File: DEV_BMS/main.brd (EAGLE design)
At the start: 93 x 70 mm, 75 parts

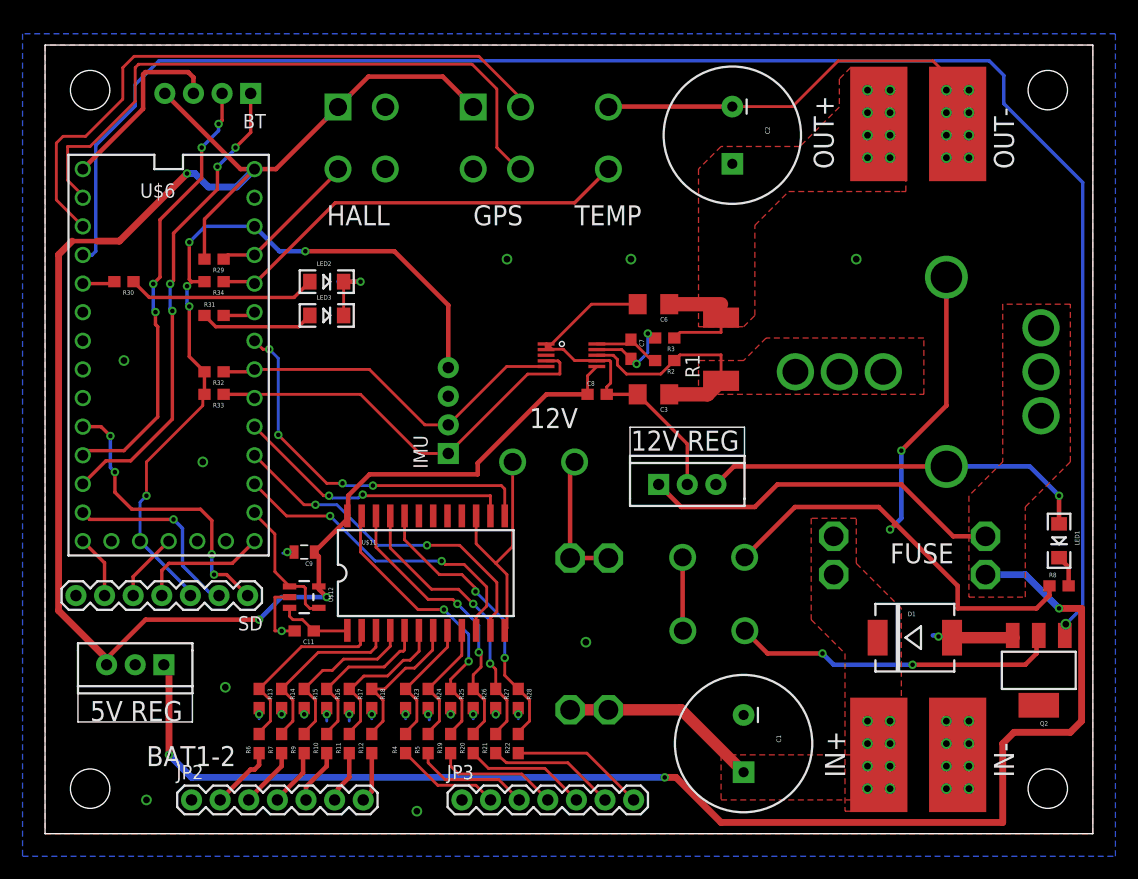
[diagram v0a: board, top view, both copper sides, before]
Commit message: new BMS with CAN and NRF24 radio
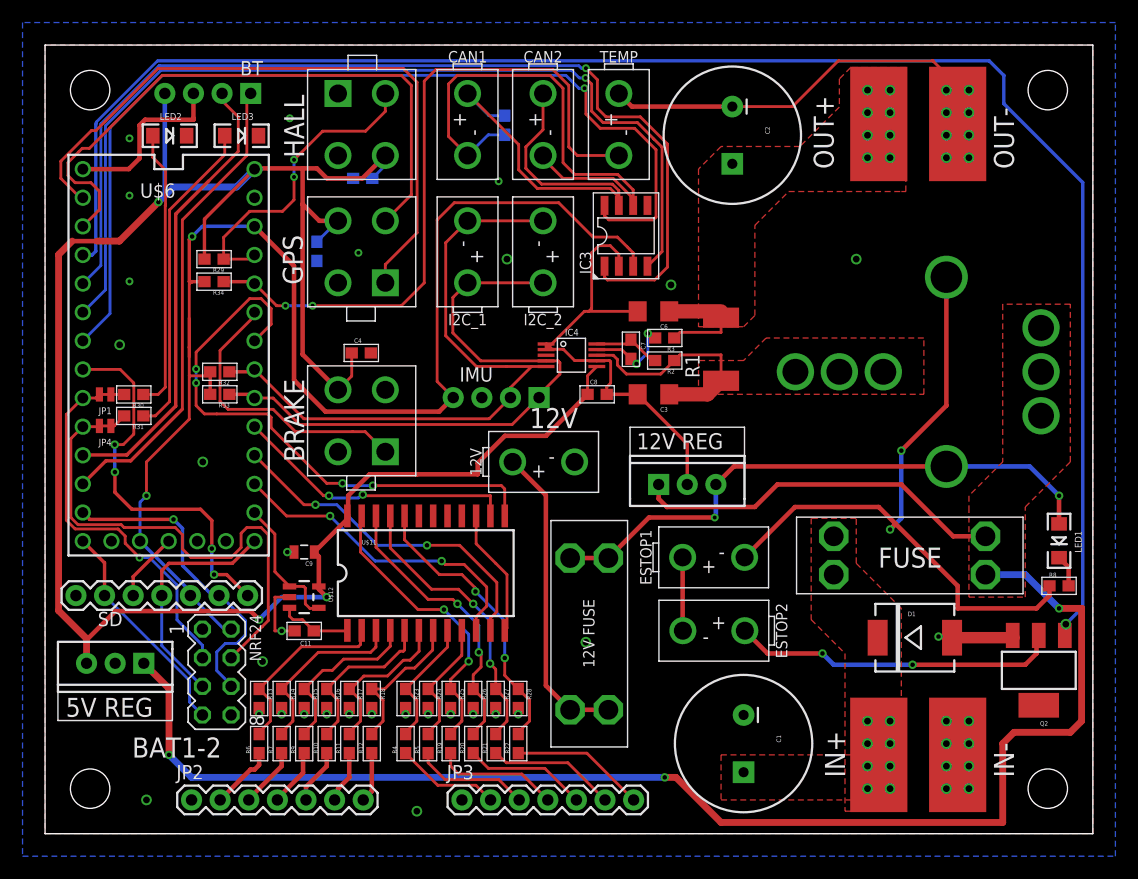
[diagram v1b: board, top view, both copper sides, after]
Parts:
- added BRAKE: HEADER4VALULOK, Custom_old:4PINVALULOK
- added C10, C5: 1uF, SparkFun-Passives:0603-CAP
- added C4: 4.7uF, SparkFun-Passives:0603-CAP
- added CAN1, CAN2, I2C_1, I2C_2, TEMP: HEADER2, Custom_old:2PINVALULOK
- added IC3: SN65HVD230D, Misaka-IC:SO-8
- added JP1, JP4: JUMPER-SMT_2_NC_TRACE_NO-SILK, SparkFun-Jumpers:SMT-JUMPER_2_NC_TRACE_NO-SILK
- added NRF24: (no value), con-lstb:MA04-2
- added R36: 120, SparkFun-Passives:0603-RES
- U$17: value HEADER2 -> (none); device Custom_old:2PINVALULOK -> Custom_old:DEV
- moved U$17 21.5 mm to (68.6, 48.3), flipped to the bottom
- moved LED2 19.0 mm to (11.1, 62.0)
- moved LED3 17.6 mm to (17.4, 62.0)
- moved R31 11.4 mm to (7.87, 37.1), turned to 180 degrees
- moved R30 10.0 mm to (7.87, 39.0)
- moved IMU 9.46 mm to (43.8, 38.7), turned to 180 degrees
- moved GPS 9.06 mm to (30.2, 54.4), turned to 180 degrees
- moved IC1 1.78 mm to (6.22, 15.1)
- moved HALL 1.20 mm to (26.0, 60.2)
- moved C6 0.63 mm to (54.0, 46.4)
- moved R32 0.51 mm to (15.5, 41.0)
- moved R33 0.51 mm to (15.5, 39.0)
- renumbered U$1 to IC4, U$10 to ESTOP2, U$19 to 12V, U$9 to ESTOP1
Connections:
- removed net N$7: IC2.OUT, LED1.A, U$7.86
- new net 12V: IC2.OUT, LED1.A, U$18.2A, U$18.2B, U$7.86
- new net BRAKE: BRAKE.1, U$6.21/A7
- new net CANH: CAN1.1, CAN2.1, IC3.7, R36.2
- new net CANL: CAN1.2, CAN2.2, IC3.6, R36.1
- new net CAN_RX: IC3.4, U$6.4
- new net CAN_TX: IC3.1, U$6.3
- new net CE: JP1.2, NRF24.3, U$6.7
- new net CSN: JP4.2, NRF24.4, U$6.8
- new net EN_CAN: IC3.8, U$6.5
- new net NRF_INT: NRF24.8
- net 3.3: now also IC3.3, NRF24.2
- net B_RAW: no longer U$18.1A, U$18.1B
- net GND: now also 12V.2, BRAKE.2, C10.2, C4.2, C5.2, GPS.3, HALL.2, IC3.2, NRF24.1, TEMP.1; no longer 12V.1, GPS.2, HALL.3, U$17.1
- net HALL: now also HALL.3; no longer HALL.2
- net LED1: now also JP1.1; no longer U$6.3
- net LED2: now also JP4.1; no longer U$6.21/A7
- net MISO: now also NRF24.7
- net MOSI: now also NRF24.6
- net N$5: now also 12V.1, U$18.1A, U$18.1B; no longer 12V.2, U$18.2A, U$18.2B
- net RX1: now also GPS.1; no longer GPS.4
- net SCK: now also NRF24.5
- net SCL: now also I2C_1.2, I2C_2.2
- net SDA: now also I2C_1.1, I2C_2.1
- net SD_CS: now also U$6.6; no longer U$6.8
- net THERMISTOR: now also TEMP.2; no longer U$17.2
- net TX1: now also GPS.2; no longer GPS.3
- net VCC: now also BRAKE.4, C10.1, C4.1, C5.1, GPS.4, HALL.4; no longer GPS.1, HALL.1
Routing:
- net CAN_TX: track 0.00 -> 89.7 mm, vias 0 -> 1
- net EN_CAN: track 0.00 -> 86.0 mm, vias 0 -> 1
- net CAN_RX: track 0.00 -> 84.2 mm, vias 0 -> 1
- net 12V: track 0.00 -> 52.0 mm, vias 0 -> 2
- net 3.3: track 69.6 -> 120.1 mm, vias 5 -> 2
- net CANL: track 0.00 -> 47.1 mm
- net CSN: track 0.00 -> 44.2 mm
- net CANH: track 0.00 -> 40.4 mm
- net N$7: track 34.7 -> 0.00 mm, vias 1 -> 0
- net CE: track 0.00 -> 33.0 mm, vias 0 -> 1
- net SCL: track 32.9 -> 58.9 mm
- net BRAKE: track 0.00 -> 25.7 mm
- net THERMISTOR: track 38.4 -> 61.7 mm, vias 0 -> 2
- net VCC: track 165.1 -> 186.7 mm
- net N$20: track 10.2 -> 28.5 mm
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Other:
- board text added: "12V FUSE"
- board text added: "BRAKE"
- board text added: "Duke Electric Vehicles, BMS 3 Designed March 29, 2017 by PLG Revised Feb 20, 2019 by GDC"
- board text added: "I kept these separate to keep the CAN line path linear"
- board text removed: "Duke Electric Vehicles, BMS 2 Designed 3/29/2017 by PLG"
- board text removed: "TEMP"
